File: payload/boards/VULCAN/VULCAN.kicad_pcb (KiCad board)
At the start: 2 copper layers, 63.5 x 101.6 mm, 58 parts, among them J1 POWER, J2 I2C, J3 Serial, J4 SPI, J5 GPIO, J6 XT60PW-M, J7 Screw_Terminal_01x06, J8 Screw_Terminal_01x06, J9 FAN, Q1 2N7002K, U1 DS18B20, U2 MPXV7002DP, U3 NJM7805SDL1-TE1, U4 AP63357, U5 DEV-16771, U6 L78M12CDT-TR, U7 MAX31855KASA, U8 MAX31855KASA, U9 MAX31855KASA

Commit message: upd
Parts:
- removed the C11 at (188.2, 48.5)
- removed the C12 at (200.9, 48.5)
- removed the U6 at (194.6, 52.7)
- added D3: OSRAM_LSR976-NR-1, Skyhawkson_Footprints:OSRAM_0805, F.Cu at (212.3, 100.1)
- added R8: R, Resistor_SMD:R_0805_2012Metric_Pad1.20x1.40mm_HandSolder, B.Cu at (211.3, 68.6)
- J9: footprint Connector_PinHeader_2.54mm:PinHeader_1x02_P2.54mm_Vertical -> Connector_Molex:Molex_KK-254_AE-6410-02A_1x02_P2.54mm_Vertical
- moved D2 3.05 mm to (212.3, 96.8)
- moved D1 0.28 mm to (170.2, 75.2)
- turned J9 to -90 degrees
- renumbered C13 to C11, C14 to C12, C15 to C13, C16 to C14, C17 to C15, C18 to C16, R9 to R10, R8 to R9, TP2 to TP1, TP1 to TP2, U3 to U2, U2 to U3, U7 to U6, U8 to U7, U9 to U8
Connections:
- J1 pad 1: /+VCC -> /+12V
- J7 pad 4: /+VCC -> /+12V
- JP1 pad 2: /+VCC -> /+12V
- R9 pad 1: /+VCC -> /+12V
- TP2 pad 1: /+VCC -> /+12V
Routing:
- net /+VCC: track 87.2 -> 0.00 mm, vias 1 -> 0
- net /+12V: track 21.7 -> 84.9 mm, vias 0 -> 1
- net Net-(D3-PadA): track 0.00 -> 32.8 mm, vias 0 -> 1
- net Net-(D2-PadA): track 17.5 -> 15.5 mm
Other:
- board text added: "+12V"
- board text added: "12V"
- board text added: "FAN"
- board text added: "VULCAN"
- board text removed: "BATT+"
- board text removed: "BATT-"
- board text removed: "VCC"

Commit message: updates
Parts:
- added JP3: Jumper_2_Open, Jumper:SolderJumper-2_P1.3mm_Open_RoundedPad1.0x1.5mm, F.Cu at (133.7, 78.0)
- added R11: 1K, Resistor_SMD:R_0805_2012Metric_Pad1.20x1.40mm_HandSolder, F.Cu at (133.9, 65.9)
- added R12: 1K, Resistor_SMD:R_0805_2012Metric_Pad1.20x1.40mm_HandSolder, F.Cu at (133.9, 68.8)
- added R13: 5K, Resistor_SMD:R_0805_2012Metric_Pad1.20x1.40mm_HandSolder, F.Cu at (133.9, 71.8)
- added R14: 5K, Resistor_SMD:R_0805_2012Metric_Pad1.20x1.40mm_HandSolder, F.Cu at (133.9, 74.7)
- added R_Shunt1: 0.1, Package_TO_SOT_SMD:TO-263-2_TabPin1, B.Cu at (139.2, 103.2)
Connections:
- net /+BATT renamed /+BATT_RAW
- J7 pad 4: /+12V -> /+12V_RAW
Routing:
- net /+12V: track 84.9 -> 73.8 mm
- net Net-(D3-PadA): track 32.8 -> 32.2 mm
- net /+BATT_RAW: track 43.7 -> 43.1 mm
- net 5V_LDO: track 8.84 -> 8.31 mm
- net /VBAT_SENSE: track 31.5 -> 31.0 mm

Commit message: updates
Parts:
- added IC1: LT1001CS8#PBF, Amplifier_Operational_Analog:Analog_LT1001_CS8, B.Cu at (156.2, 112.5)
- JP3: moved to B.Cu
- moved R12 51.9 mm to (156.0, 115.8)
- moved R11 50.9 mm to (156.0, 111.8)
- moved R13 47.4 mm to (156.0, 113.8)
- moved R14 41.4 mm to (156.0, 109.7)
- moved R_Shunt1 32.0 mm to (169.8, 112.5), turned to 0 degrees
- moved JP3 31.4 mm to (161.8, 91.9), turned to 180 degrees
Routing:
- net /+12V: track 73.8 -> 107.5 mm
- net /+12V_RAW: track 0.00 -> 25.0 mm
- net /I2C_SDA: track 28.1 -> 34.3 mm
- net /I2C_SCL: track 24.6 -> 30.7 mm
- net +3V3: vias 5 -> 6
- net /LED_GREEN: vias 2 -> 3
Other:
- board text added: "SHUNT BYPASS"

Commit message: updates
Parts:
- BT1: footprint Battery:BatteryHolder_Keystone_3002_1x2032 -> Battery:BatteryHolder_Keystone_1060_1x2032
- C1: value 0.33uF -> 22uF
- C8: value 0.1uF -> 10uF
- IC1, R1: moved to F.Cu
- R11, R12, R13, R14: moved to B.Cu
- R_Shunt1: value 0.1 -> 0.05; footprint Package_TO_SOT_SMD:TO-263-2_TabPin1 -> Resistor_SMD:R_2816_7142Metric_Pad3.20x4.45mm_HandSolder
- U2: value NJM7805SDL1-TE1 -> AZ1117IH-5.0TRG1; footprint CustomFootprintLib:TO-252-3-L1_NMD -> CustomFootprintLib:SOT223-5_DIO
- moved R_Shunt1 21.6 mm to (165.1, 91.4), turned to 180 degrees
- moved R12 14.1 mm to (169.7, 112.5), turned to -90 degrees
- moved R10 13.8 mm to (179.6, 94.2), turned to 180 degrees
- moved U2 13.5 mm to (177.3, 78.7), turned to 180 degrees
- moved R14 12.0 mm to (167.6, 112.5), turned to 90 degrees
- moved R9 12.0 mm to (179.6, 91.9), turned to 0 degrees
- moved IC1 10.3 mm to (166.5, 112.4), turned to -90 degrees
- moved R1 10.2 mm to (170.2, 70.6)
- moved R11 9.68 mm to (165.6, 112.5), turned to -90 degrees
- moved R13 7.73 mm to (163.6, 112.5), turned to -90 degrees
- moved C8 6.88 mm to (170.9, 80.5), turned to 180 degrees
- moved JP3 5.85 mm to (165.1, 87.1)
- moved J1 4.98 mm to (172.6, 92.0)
- moved C1 4.90 mm to (170.9, 78.2), turned to 180 degrees
- moved R4 4.35 mm to (161.3, 99.8)
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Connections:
- C1 pad 1: 5V_LDO -> +5V
- C8 pad 1: +5V -> 5V_LDO
- U2 pad 1: 5V_LDO -> GND
- U2 pad 2: GND -> +5V
- U2 pad 3: +5V -> 5V_LDO
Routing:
- net /VBAT_COIN: track 60.5 -> 19.7 mm, vias 2 -> 0
- net +3V3: track 113.5 -> 91.4 mm
- net /VBAT_SENSE: track 31.0 -> 13.0 mm, vias 2 -> 0
- net /LED_GREEN: track 61.7 -> 46.6 mm
- net Net-(IC1-+IN): track 0.00 -> 12.9 mm, vias 0 -> 1
- net /+12V_RAW: track 25.0 -> 37.1 mm, vias 0 -> 1
- net Net-(IC1--IN): track 0.00 -> 9.44 mm, vias 0 -> 1
- net /DS18_TEMP: track 36.2 -> 29.1 mm
- net /T1_CS: track 44.8 -> 51.7 mm
- net /VBAT_CURRENT_SENSE: track 0.00 -> 5.74 mm, vias 0 -> 1
- net /I2C_SDA: track 34.3 -> 28.7 mm
- net /I2C_SCL: track 30.7 -> 25.3 mm
- net /+12V: track 107.5 -> 102.5 mm
- net /T2_CS: track 38.7 -> 43.4 mm
- net 5V_BUCK: track 32.4 -> 36.9 mm
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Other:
- board text added: "+3V3"
- board text added: "12V FAN ONLY"
- board text added: "CR2032"
- board text added: "Thermocouple Inputs"
- board text removed: "3V3"
- board text removed: "Heat Flow Sensor Board"

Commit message: upd
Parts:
- R9: value 200k -> 300k
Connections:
- U5 pad 15: /DS18_TEMP -> unconnected-(U5-A1-Pad15)
- U5 pad 40: unconnected-(U5-A16-Pad40) -> /DS18_TEMP
- U5 pad 41: unconnected-(U5-A17-Pad41) -> /VBAT_CURRENT_SENSE
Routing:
- net /VBAT_CURRENT_SENSE: track 5.74 -> 37.1 mm
- net /DS18_TEMP: track 29.1 -> 17.7 mm, vias 1 -> 0
- net 5V_BUCK: track 36.9 -> 31.7 mm
- net /SPI_MISO: track 70.6 -> 72.7 mm
- net /FAN: track 59.9 -> 57.8 mm, vias 2 -> 1
- net Net-(IC1--IN): track 9.44 -> 8.42 mm

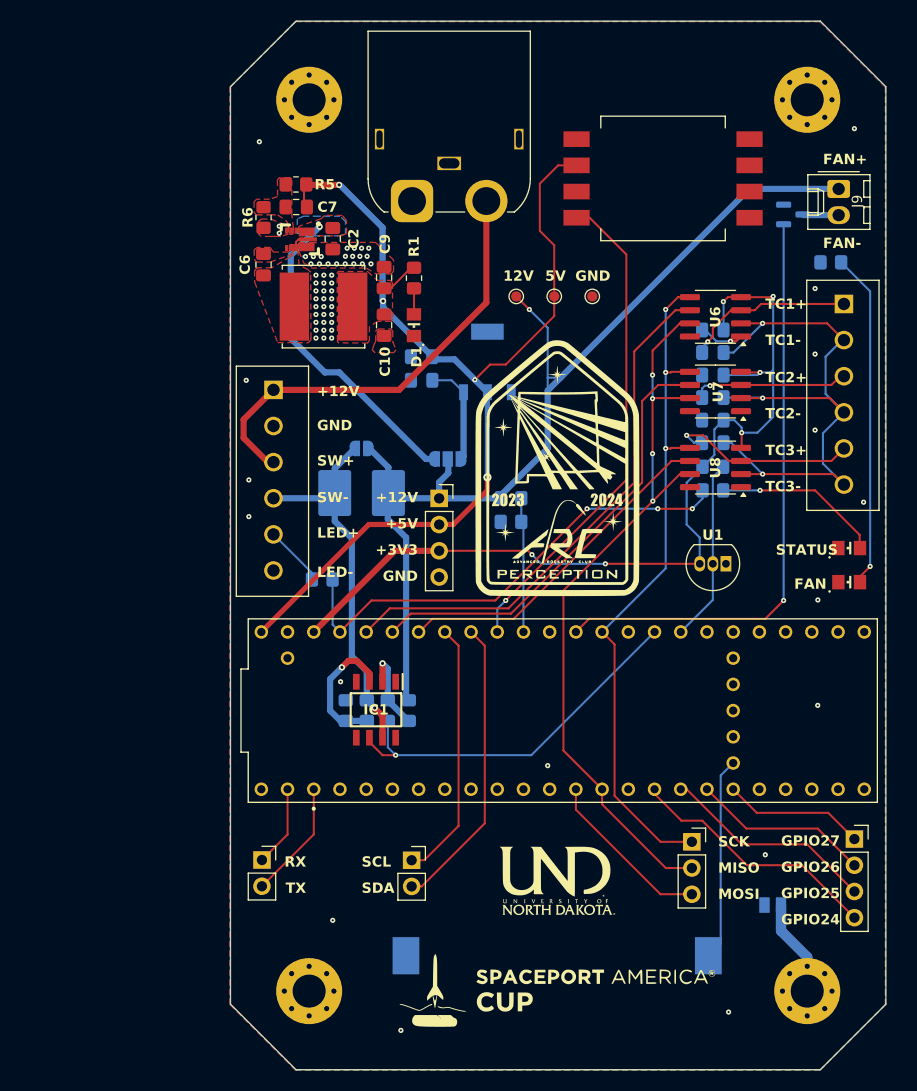
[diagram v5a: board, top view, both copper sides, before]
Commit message: updates
1-wire sensor
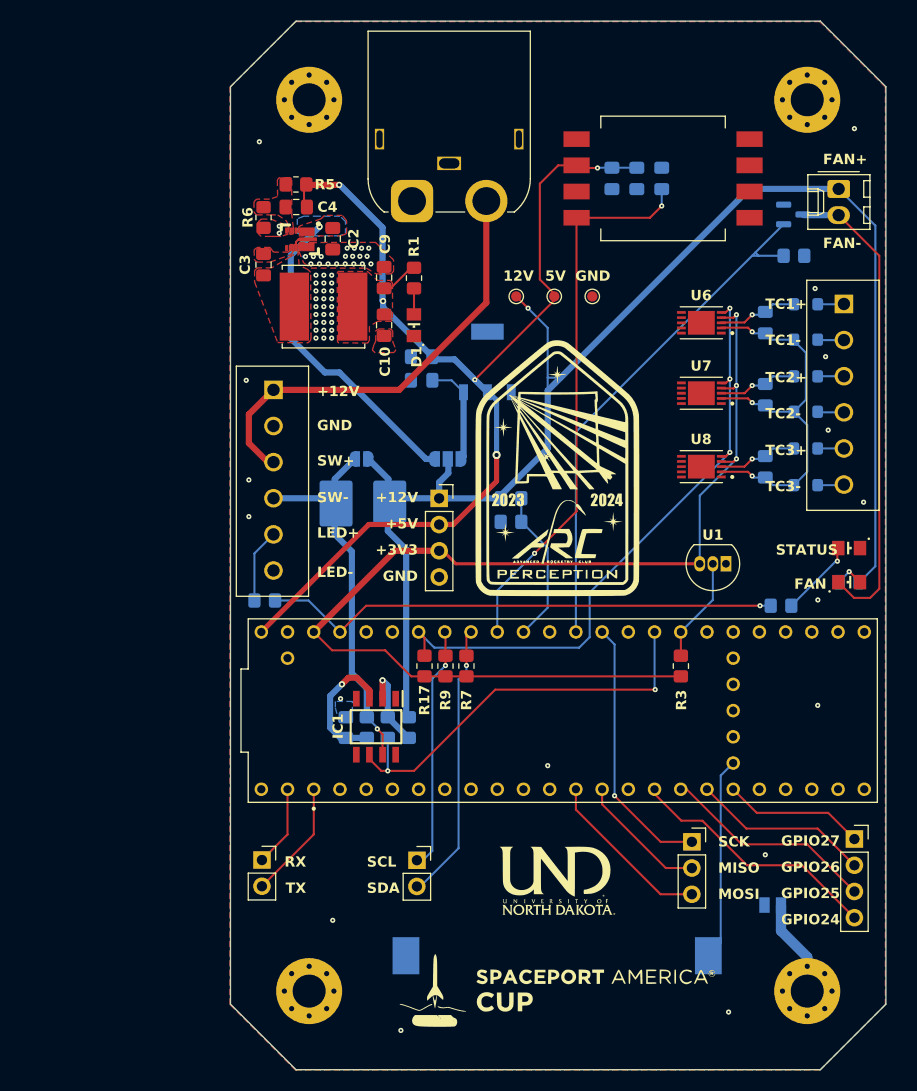
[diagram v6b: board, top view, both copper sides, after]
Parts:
- removed C14, C16: 0.1uF, Capacitor_SMD:C_0805_2012Metric_Pad1.18x1.45mm_HandSolder
- added C6: 0.1uF, Capacitor_SMD:C_0805_2012Metric_Pad1.18x1.45mm_HandSolder, B.Cu at (204.2, 74.9)
- added C7: 0.1uF, Capacitor_SMD:C_0805_2012Metric_Pad1.18x1.45mm_HandSolder, B.Cu at (204.2, 88.9)
- added FB1: Ferrite_Bead, PCM_Ferrite_SMD_AKL:Ferrite_0805_2012Metric_Pad1.05x1.20mm_BigPads, B.Cu at (208.1, 73.2)
- added FB2: Ferrite_Bead, PCM_Ferrite_SMD_AKL:Ferrite_0805_2012Metric_Pad1.05x1.20mm_BigPads, B.Cu at (208.1, 76.6)
- added FB3: Ferrite_Bead, PCM_Ferrite_SMD_AKL:Ferrite_0805_2012Metric_Pad1.05x1.20mm_BigPads, B.Cu at (208.1, 80.1)
- added FB4: Ferrite_Bead, PCM_Ferrite_SMD_AKL:Ferrite_0805_2012Metric_Pad1.05x1.20mm_BigPads, B.Cu at (208.1, 83.6)
- added FB5: Ferrite_Bead, PCM_Ferrite_SMD_AKL:Ferrite_0805_2012Metric_Pad1.05x1.20mm_BigPads, B.Cu at (208.1, 87.1)
- added FB6: Ferrite_Bead, PCM_Ferrite_SMD_AKL:Ferrite_0805_2012Metric_Pad1.05x1.20mm_BigPads, B.Cu at (208.1, 90.7)
- added R17: 4.7k, Resistor_SMD:R_0805_2012Metric_Pad1.20x1.40mm_HandSolder, F.Cu at (171.2, 108.2)
- added R7: R, Resistor_SMD:R_0805_2012Metric_Pad1.20x1.40mm_HandSolder, F.Cu at (175.3, 108.2)
- added R8: 470, Resistor_SMD:R_0805_2012Metric_Pad1.20x1.40mm_HandSolder, B.Cu at (207.0, 68.5)
- added R9: R, Resistor_SMD:R_0805_2012Metric_Pad1.20x1.40mm_HandSolder, F.Cu at (173.2, 108.2)
- C11: value 100n -> 470pF
- C12: value 100n -> 0.01uF
- C13: value 100n -> 1.0uF
- D2: value OSRAM_LGR971-KN-1 -> CMD17-21VGD/TR8
- D3: value OSRAM_LSR976-NR-1 -> CMD17-21VGD/TR8
- J9: footprint Connector_Molex:Molex_KK-254_AE-6410-02A_1x02_P2.54mm_Vertical -> CustomFootprintLib:Molex_KK-254_AE-6410-02A_1x02_P2.54mm_Vertical
- R1: value R -> 150
- R10: renamed from R8; value R -> 500
- R2: value R -> 68
- R3: moved to F.Cu
- U6, U7, U8: value MAX31855KASA -> MAX31850KATB+T; footprint Package_SO:SOIC-8_3.9x4.9mm_P1.27mm -> CustomFootprintLib:SON50P300X400X80-11N
- moved R10 31.0 mm to (212.3, 100.1), turned to 180 degrees
- moved C13 26.6 mm to (191.8, 61.0), turned to -90 degrees
- moved C12 23.4 mm to (189.4, 61.0), turned to -90 degrees
- moved R3 19.6 mm to (196.0, 108.2), turned to 90 degrees
- moved C11 17.6 mm to (194.2, 61.0), turned to 90 degrees
- moved R2 13.0 mm to (205.7, 102.4)
- moved R4 5.93 mm to (155.7, 101.9)
- moved C8 5.43 mm to (204.2, 81.9), turned to -90 degrees
- moved IC1 1.64 mm to (166.5, 114.1)
- moved R13 1.64 mm to (165.6, 114.2)
- moved R14 1.64 mm to (169.7, 114.2)
- moved R15 1.64 mm to (163.6, 114.2)
- moved R16 1.64 mm to (167.6, 114.2)
- moved U6 1.48 mm to (198.0, 74.9)
- moved U7 1.38 mm to (198.0, 81.8)
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- renumbered C6 to C3, C7 to C4, C8 to C5, C15 to C8, R9 to R11, R10 to R12, R11 to R13, R12 to R14, R13 to R15, R14 to R16, U4 to U3, U3 to U4
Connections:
- C11 pad 1: /T1 -> /PITOT
- C11 pad 2: /T- -> GND
- C12 pad 1: /T2 -> +5V
- C12 pad 2: /T- -> GND
- C13 pad 1: /T3 -> +5V
- C13 pad 2: /T- -> GND
- C8 pad 1: +3V3 -> /T2
- C8 pad 2: GND -> /T-
- D3 pad C: GND -> Net-(J9-Pin_2)
- J8 pad 1: /T1 -> Net-(J8-Pin_1)
- J8 pad 2: /T- -> Net-(J8-Pin_2)
- J8 pad 3: /T2 -> Net-(J8-Pin_3)
- J8 pad 4: /T- -> Net-(J8-Pin_4)
- J8 pad 5: /T3 -> Net-(J8-Pin_5)
- J8 pad 6: /T- -> Net-(J8-Pin_6)
- R10 pad 1: GND -> /+12V
- U5 pad 20: /T3_CS -> /TC_DATA
- U5 pad 21: /T2_CS -> unconnected-(U5-A7-Pad21)
- U5 pad 22: /T1_CS -> unconnected-(U5-A8-Pad22)
- U6 pad 5: /SPI_SCK -> /TC_DATA
- U6 pad 6: /T1_CS -> unconnected-(U6-AD0-Pad6)
- U6 pad 7: /SPI_MISO -> unconnected-(U6-AD1-Pad7)
- U6 pad 8: (no net) -> unconnected-(U6-AD2-Pad8)
- U7 pad 5: /SPI_SCK -> /TC_DATA
- U7 pad 6: /T2_CS -> unconnected-(U7-AD0-Pad6)
- U7 pad 7: /SPI_MISO -> unconnected-(U7-AD1-Pad7)
- U7 pad 8: (no net) -> unconnected-(U7-AD2-Pad8)
- U8 pad 5: /SPI_SCK -> /TC_DATA
- U8 pad 6: /T3_CS -> unconnected-(U8-AD0-Pad6)
- U8 pad 7: /SPI_MISO -> unconnected-(U8-AD1-Pad7)
- U8 pad 8: (no net) -> unconnected-(U8-AD2-Pad8)
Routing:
- net /SPI_MISO: track 72.7 -> 12.0 mm, vias 4 -> 0
- net /TC_DATA: track 0.00 -> 60.7 mm, vias 0 -> 3
- net /T1_CS: track 51.7 -> 0.00 mm
- net /T2_CS: track 43.4 -> 0.00 mm
- net Net-(J9-Pin_2): track 3.38 -> 46.2 mm
- net /SPI_SCK: track 67.1 -> 25.7 mm, vias 3 -> 1
- net /+12V: track 102.5 -> 142.8 mm
- net /T3_CS: track 33.1 -> 0.00 mm
- net Net-(D3-PadA): track 32.0 -> 2.90 mm
- net /T-: track 62.5 -> 38.6 mm
- net +3V3: track 91.4 -> 108.5 mm, vias 6 -> 3
- net /T3: track 18.6 -> 7.39 mm
- net Net-(D2-PadA): track 16.2 -> 7.27 mm
- net /T1: track 16.0 -> 7.40 mm
- net /DS18_TEMP: track 17.7 -> 10.2 mm
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
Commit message: updates
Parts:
- moved JP1 0.76 mm to (172.7, 88.1)
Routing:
- net 5V_BUCK: track 31.7 -> 30.9 mm

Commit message: updates
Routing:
- net /VBAT_SENSE: track 15.0 -> 13.0 mm
- net +5V: track 106.6 -> 105.8 mm
